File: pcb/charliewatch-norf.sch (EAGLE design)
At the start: 84 parts, among them U2 CC430F5137IRGZR, X1 CRYSTALS-NOGND-IQXC-25

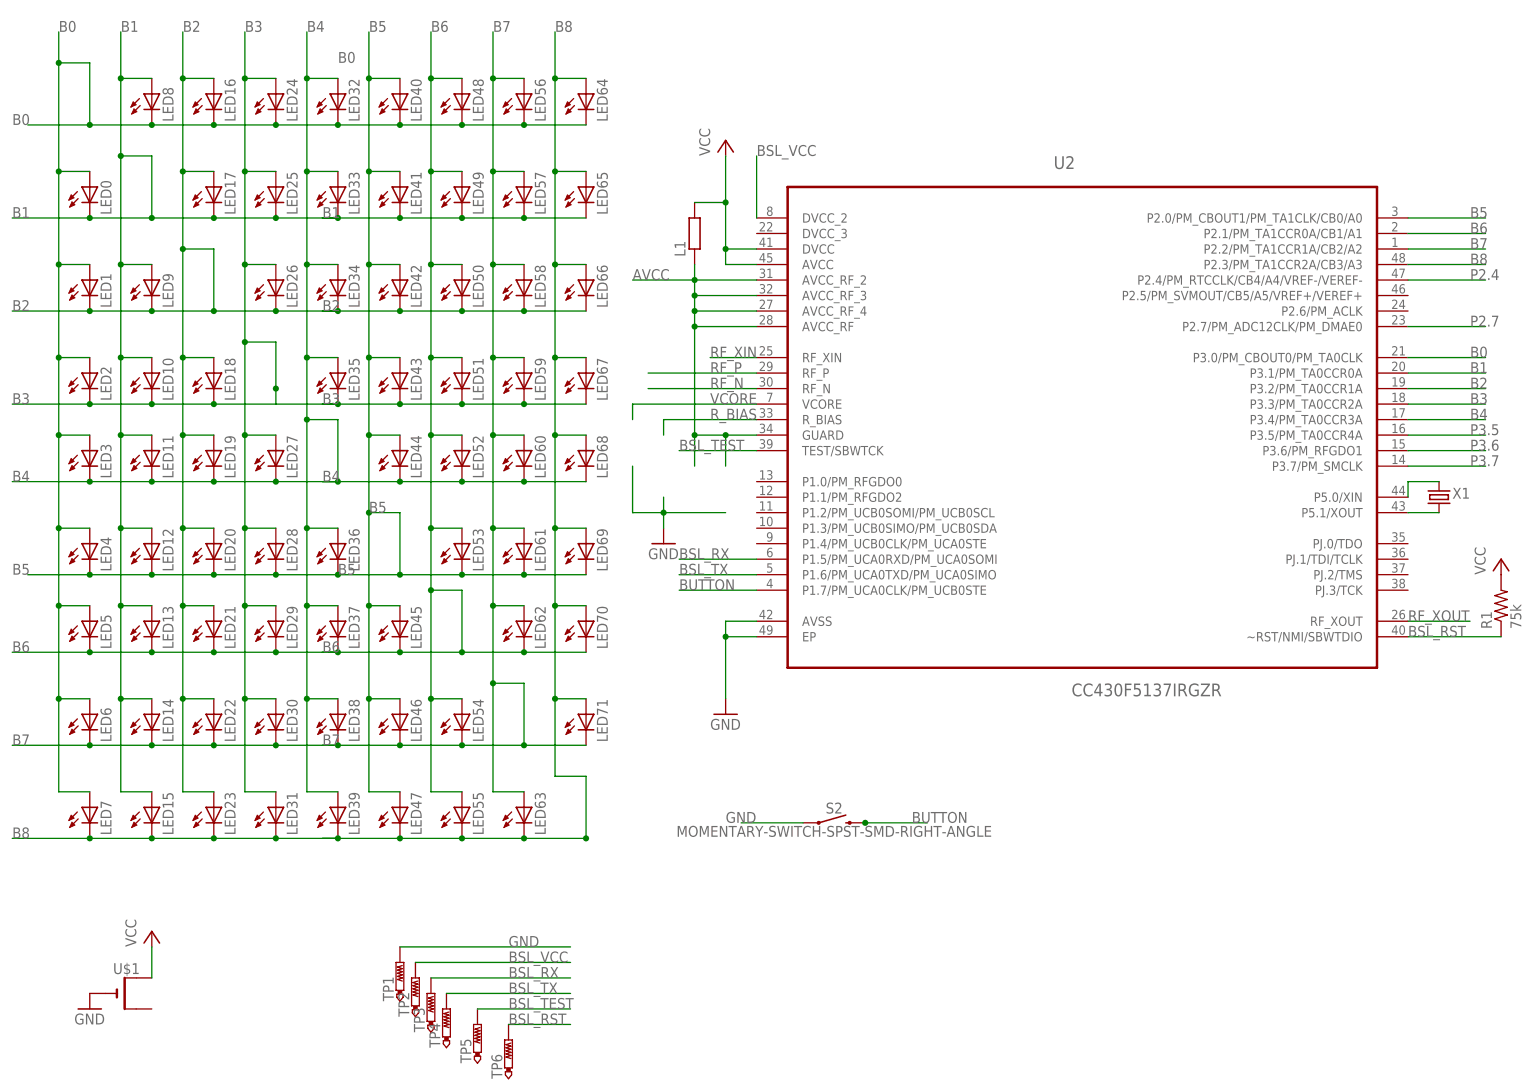
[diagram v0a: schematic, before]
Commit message: Add LIS3DH Accelerometer
LIS3DH is an i2c accelerometer. Hope to use this to control the watch
with tap based gestures
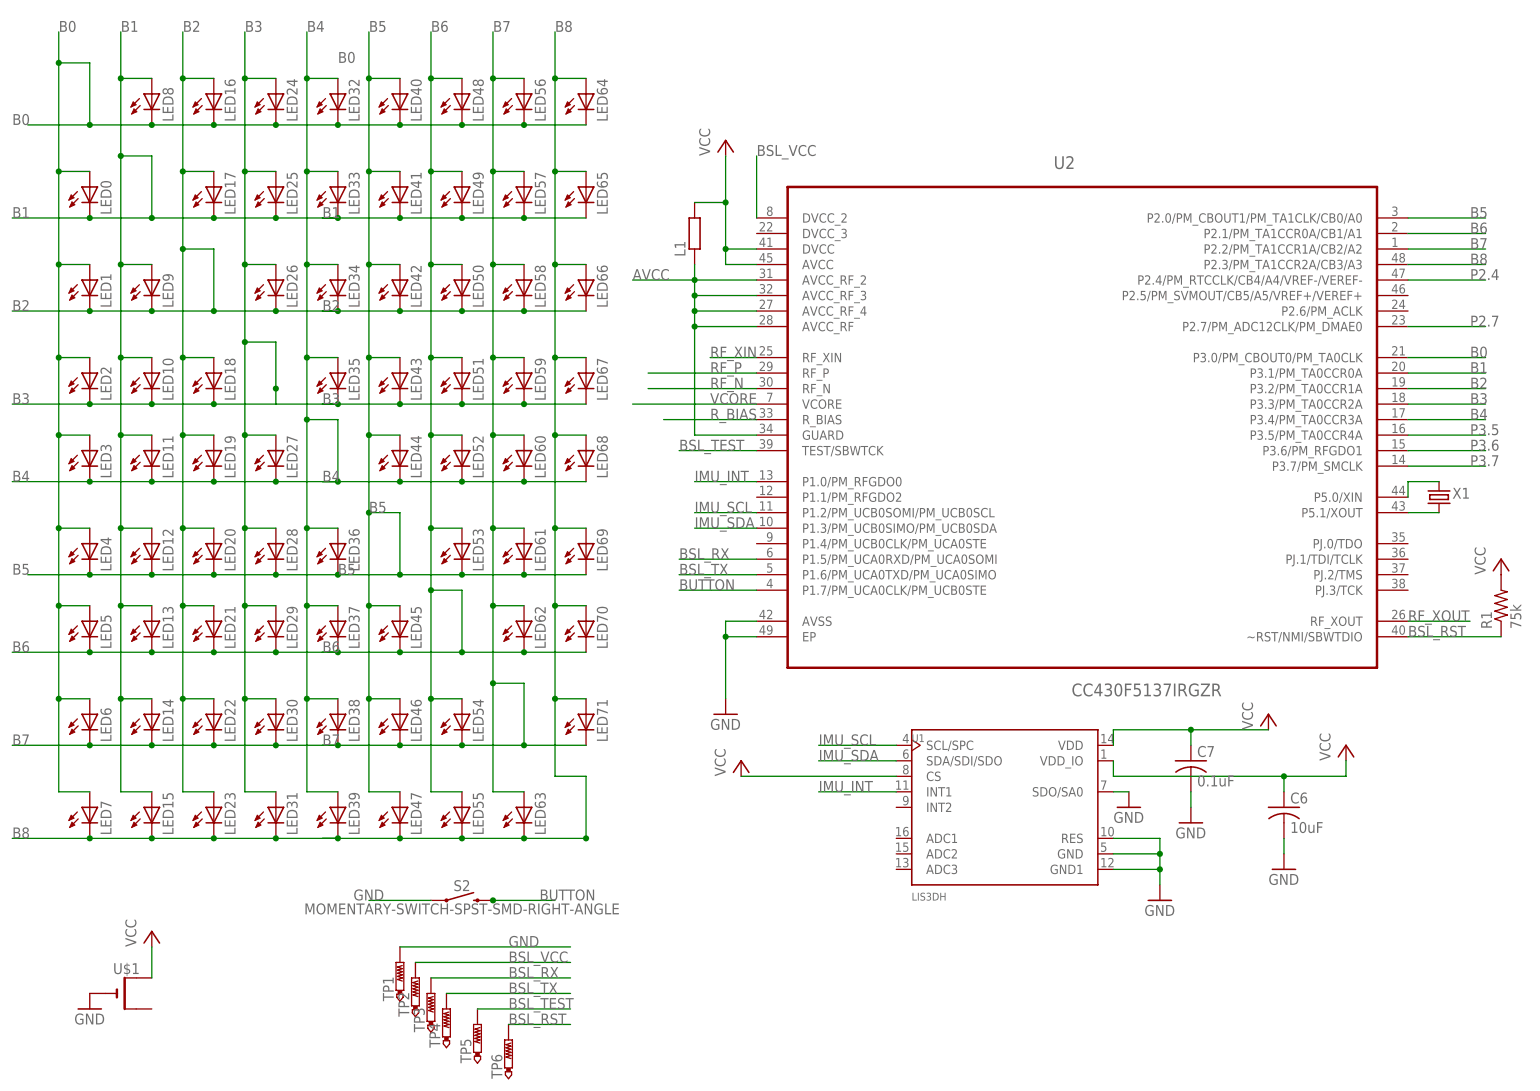
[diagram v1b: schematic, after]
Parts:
- added C6: 10uF, resistor:C-USC0603
- added C7: 0.1uF, resistor:C-USC0603
- added U1: LIS3DH, LIS3DH:LIS3DH
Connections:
- new net IMU_INT: U1.INT1, U2.P1.0/PM_RFGDO0
- new net IMU_SCL: U1.SCL/SPC, U2.P1.2/PM_UCB0SOMI/PM_UCB0SCL
- new net IMU_SDA: U1.SDA/SDI/SDO, U2.P1.3/PM_UCB0SIMO/PM_UCB0SDA
- net GND: now also C6.2, C7.2, U1.GND, U1.GND1, U1.RES, U1.SDO/SA0
- net VCC: now also C6.1, C7.1, U1.CS, U1.VDD, U1.VDD_IO
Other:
- moved on the sheet: S2

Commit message: Cleaned up .brd File
The Origin of the watch is (20, 20). Can now reference from that point
when designing
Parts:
- removed L1: (no value), rcl:R-EU_R0603
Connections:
- net AVCC: no longer L1.1
- net VCC: no longer L1.2
